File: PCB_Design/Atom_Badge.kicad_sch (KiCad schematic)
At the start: 57 parts

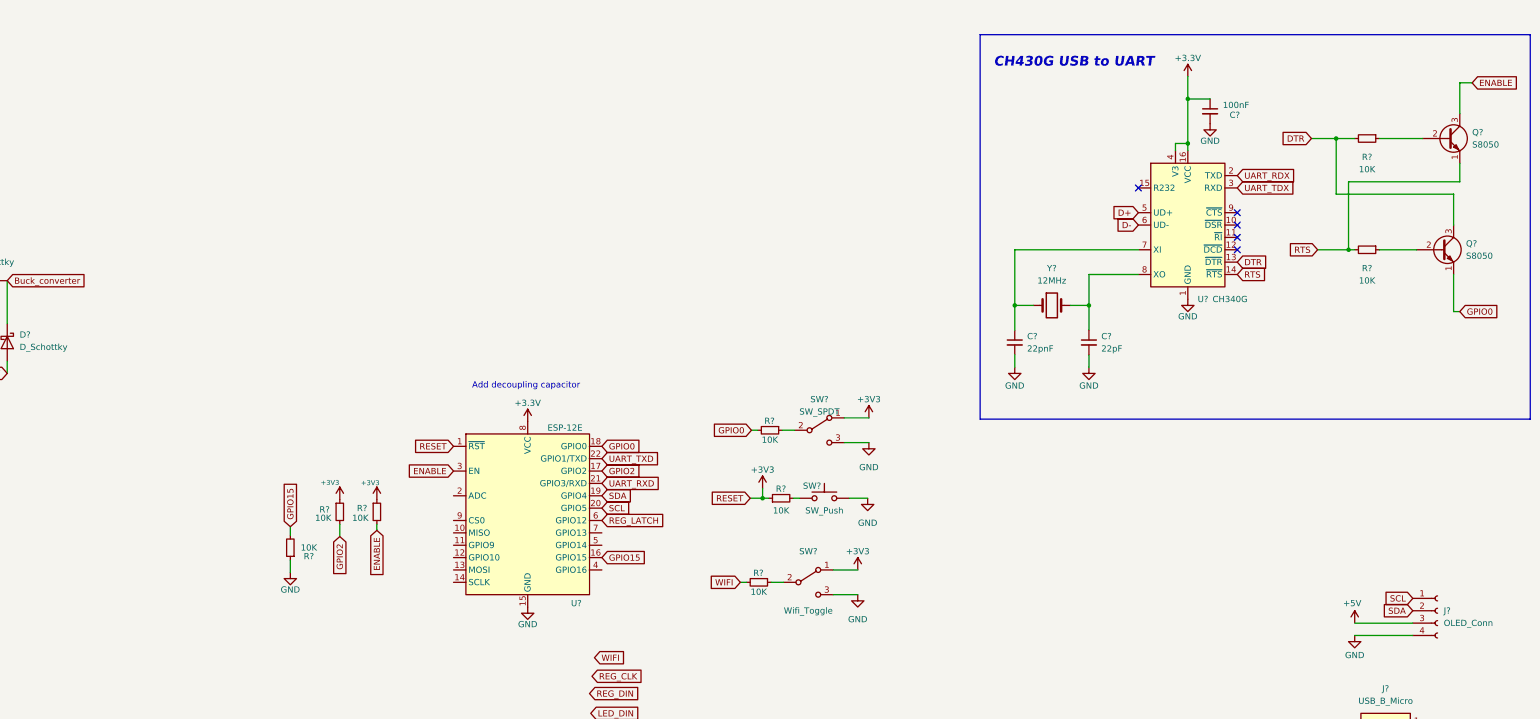
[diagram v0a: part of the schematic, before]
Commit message: added adc
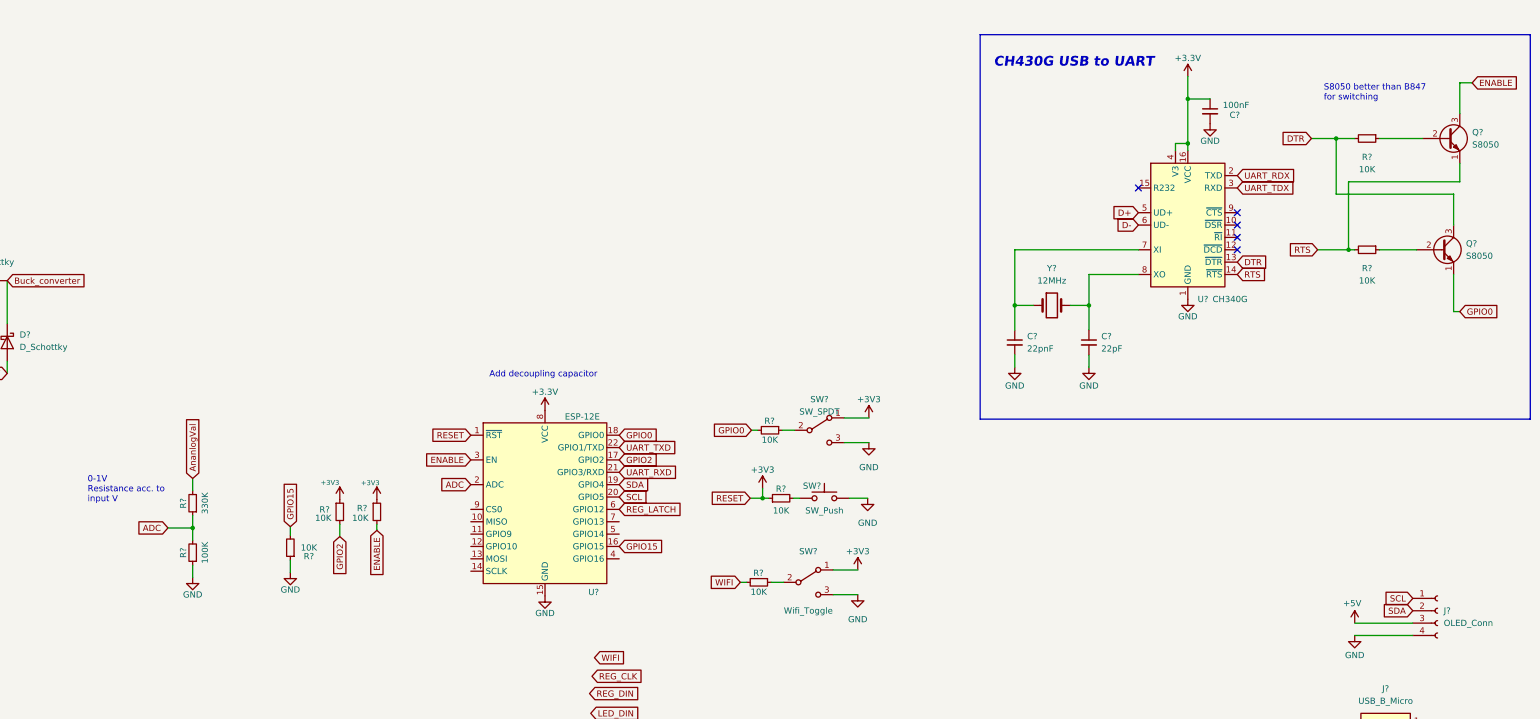
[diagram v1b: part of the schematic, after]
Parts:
- added R?: 330K, Resistor_SMD:R_1206_3216Metric_Pad1.30x1.75mm_HandSolder, symbol Device:R_Small
- added R?: 100K, Resistor_SMD:R_1206_3216Metric_Pad1.30x1.75mm_HandSolder, symbol Device:R_Small
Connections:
- net GND: now also R?.1
- net ADC: now reaches U?.2 (ADC)
- net ADC: now also R?.1, R?.2
- new net AnanlogVal: R?.2
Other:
- note added: "0-1V Resistance acc. to input V"
- note added: "S8050 better than B847 for switching"
- moved on the sheet: U?

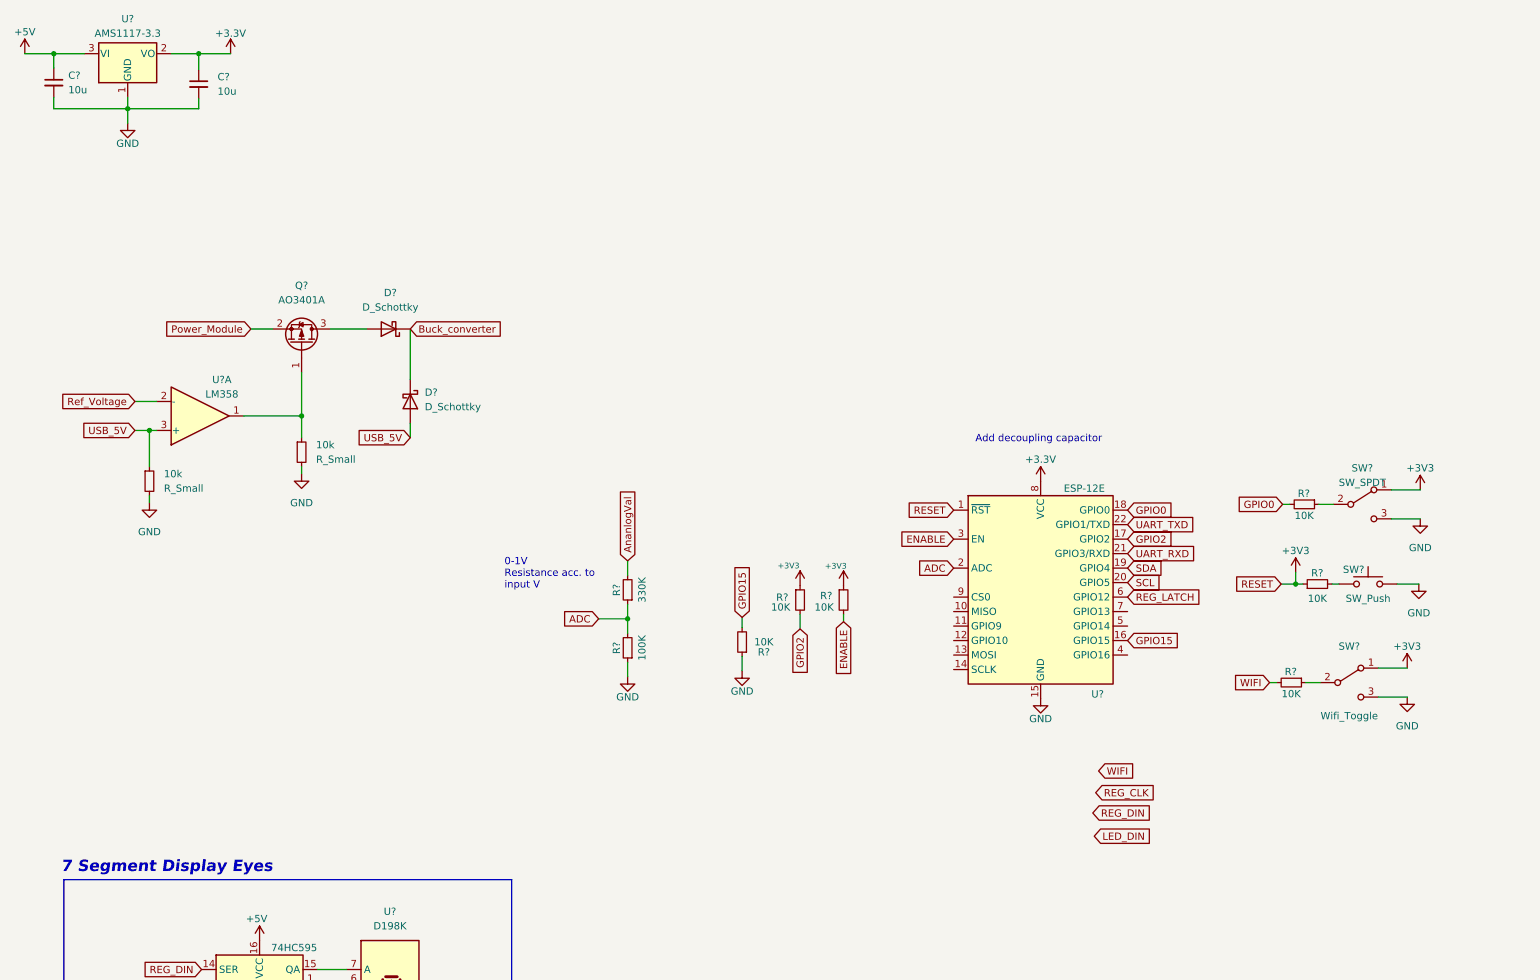
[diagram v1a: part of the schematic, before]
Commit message: Added power bank module symbol & footprint
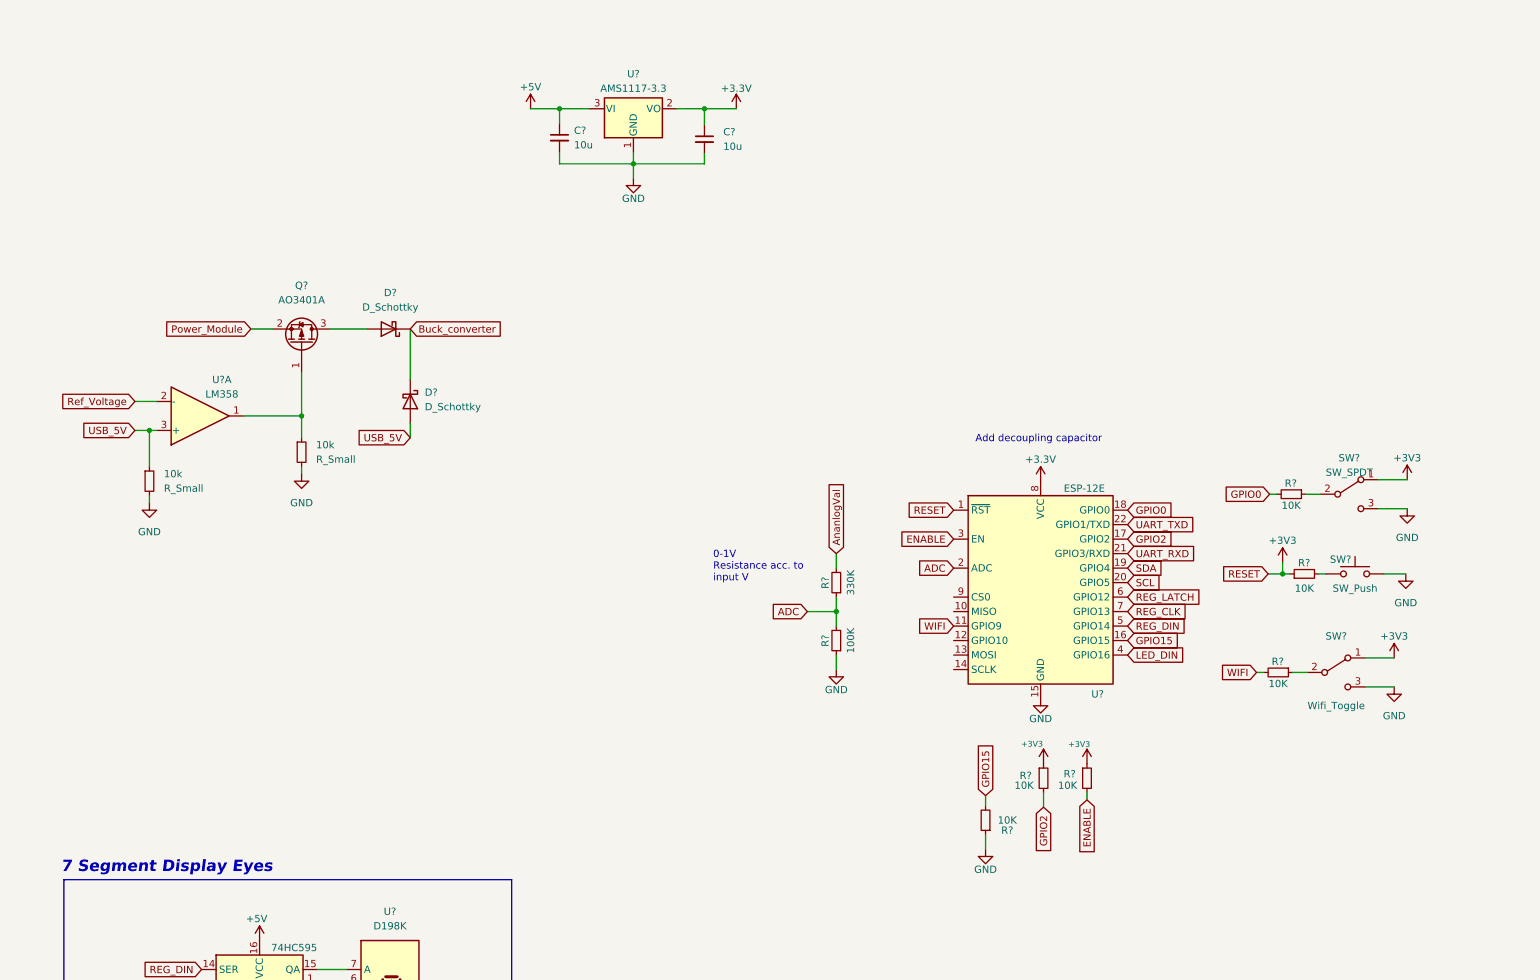
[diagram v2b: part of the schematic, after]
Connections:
- net LED_DIN: now also U?.4 (GPIO16)
- net REG_CLK: now also U?.7 (GPIO13)
- net REG_DIN: now also U?.5 (GPIO14)
- net WIFI: now also U?.11 (GPIO9)
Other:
- moved on the sheet: C?, R?, SW?, U?

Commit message: Completed & Annotated Schematic
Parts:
- added U1: T6845C_Module, symbol Power_Bank_Module:T6845C_Module
- SW2: renamed from SW?; value SW_SPDT -> Boot
- SW3: renamed from SW?; value SW_Push -> RST
- gave numbers to parts that had none: 55
- renumbered 10k to 10k1, 10k to 10k2
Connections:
- net Power_Module is gone; now on net +5V: Q2.2 (S)
- net Ref_Voltage is gone; now on net VBAT+: U6.2 (-)
- net +5V: now also U1.5 (OUT+); no longer C8.1, U7.3 (VI)
- net GND: now also U1.4 (B-), U1.6 (OUT-)
- net AnanlogVal renamed VBAT+
- net VBAT+: now also U1.3 (B+)
- net Buck_converter renamed AMS_Vin
- net AMS_Vin: now also C8.1, U7.3 (VI)
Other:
- note added: "ESP12-E Core"
- note added: "Power Management & Distribution Block"
- note added: "Select higher value for less power draw maybe"
- moved on the sheet: 10k1, 10k2, C1, C10, C11, C12, C13, C14, C15, C16, C2, C3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

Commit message: added footprint
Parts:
- 10k1, 10k2, R10, R11, R4: footprint (none) -> Resistor_SMD:R_1206_3216Metric_Pad1.30x1.75mm_HandSolder
- C10, C14, C15, C8: footprint (none) -> Capacitor_SMD:C_1206_3216Metric_Pad1.33x1.80mm_HandSolder
- C16: footprint (none) -> Connector_USB:USB_Micro-B_Wuerth_629105150521_CircularHoles
- D4, D6: value D_Schottky -> SS34; footprint (none) -> Diode_SMD:D_2512_6332Metric_Pad1.52x3.35mm_HandSolder
- J1: footprint (none) -> Connector_USB:USB_Micro-AB_Molex_47590-0001
- J2: footprint (none) -> Connector_PinSocket_2.54mm:PinSocket_1x04_P2.54mm_Vertical
- U2, U3: footprint (none) -> Package_DIP:DIP-16_W7.62mm
- U6: footprint (none) -> Package_DIP:DIP-8_W7.62mm
- Y1: footprint (none) -> Crystal:Crystal_HC18-U_Vertical
